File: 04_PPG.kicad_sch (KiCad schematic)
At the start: 0 parts

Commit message: updated schematics
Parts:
- added C4101, C4201: 22uF, Capacitor_SMD:C_0402_1005Metric, symbol Device:C
- added C4102, C4202: 100nF, Capacitor_SMD:C_0402_1005Metric, symbol Device:C
- added C4103, C4203: 1.0uF, Capacitor_SMD:C_0402_1005Metric, symbol Device:C
- added C4104, C4204: 10uF, Capacitor_SMD:C_0402_1005Metric, symbol Device:C
- added D401, D402: SFH7018A Q65113A6157, symbol sportwatch_custom:SFH7018A
- added D413, D414, D423, D424: SFH2703H Q65115A2199, symbol sportwatch_custom:SFH2703H
- added NT401: PPG1_PD_GND_TIE, symbol sportwatch_custom:NetTie_2
- added NT402: PPG2_PD_GND_TIE, symbol sportwatch_custom:NetTie_2
- added R401, R402, R405: 100k, Resistor_SMD:R_0402_1005Metric, symbol Device:R
- added R403, R404: 47k, Resistor_SMD:R_0402_1005Metric, symbol Device:R
- added U12, U13: MAX86141ENP+T, 21-100134_N201A2-1_MXM, symbol 2026-09-16_07-42-39:MAX86141ENP+T
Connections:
- new net GND: C4101.2, C4102.2, C4103.2, C4104.2, C4201.2, C4202.2, C4203.2, C4204.2, NT401.2 (B), NT402.2 (B), U12.C3 (GND_DIG), U12.C4 (GND_ANA), U12.D3 (PGND), U13.C3 (GND_DIG), U13.C4 (GND_ANA), U13.D3 (PGND)
- new net PPG1_CS_N: R401.2, U12.A5 (CSB)
- new net PPG1_INT_N: R403.2, U12.B2 (*INT)
- new net PPG1_LED_GREEN_DRV: D401.1 (K_GREEN_1), D401.8 (K_GREEN_3), U12.D1 (LED1_DRV)
- new net PPG1_LED_IR_DRV: D401.3 (K_IR), U12.B1 (LED3_DRV)
- new net PPG1_LED_RED_DRV: D401.5 (K_RED), U12.C1 (LED2_DRV)
- new net PPG1_PD1_IN: D413.1 (CATHODE), U12.D5 (PD1_IN)
- new net PPG1_PD2_IN: D414.1 (CATHODE), U12.D4 (PD2_IN)
- new net PPG1_PD_GND: D413.2 (ANODE), D414.2 (ANODE), NT401.1 (A), U12.C5 (PD_GND)
- new net PPG1_VREF: C4103.1, U12.B5 (VREF)
- new net PPG2_CS_N: R402.2, U13.A5 (CSB)
- new net PPG2_INT_N: R404.2, U13.B2 (*INT)
- new net PPG2_LED_GREEN_DRV: D402.1 (K_GREEN_1), D402.8 (K_GREEN_3), U13.D1 (LED1_DRV)
- new net PPG2_LED_IR_DRV: D402.3 (K_IR), U13.B1 (LED3_DRV)
- new net PPG2_LED_RED_DRV: D402.5 (K_RED), U13.C1 (LED2_DRV)
- new net PPG2_PD1_IN: D423.1 (CATHODE), U13.D5 (PD1_IN)
- new net PPG2_PD2_IN: D424.1 (CATHODE), U13.D4 (PD2_IN)
- new net PPG2_PD_GND: D423.2 (ANODE), D424.2 (ANODE), NT402.1 (A), U13.C5 (PD_GND)
- new net PPG2_VREF: C4203.1, U13.B5 (VREF)
- new net PPG_SAMPLE_SYNC: R405.2, U12.B3 (GPIO1), U13.B3 (GPIO1)
- new net PPG_SPI_MISO: U12.A3 (SDO), U13.A3 (SDO)
- new net PPG_SPI_MOSI: U12.A4 (SDI), U13.A4 (SDI)
- new net PPG_SPI_SCLK: U12.A2 (SCLK), U13.A2 (SCLK)
- new net PPG_VLED: C4104.1, C4204.1, D401.2 (A_RED_IR_1), D401.4 (A_RED_IR_2), D401.6 (A_GREEN), D402.2 (A_RED_IR_1), D402.4 (A_RED_IR_2), D402.6 (A_GREEN), U12.A1 (VLED), U13.A1 (VLED)
- new net VOUT1_1V8: C4101.1, C4102.1, C4201.1, C4202.1, R401.1, R402.1, R403.1, R404.1, R405.1, U12.C2 (VDD_DIG), U12.D2 (VDD_ANA), U13.C2 (VDD_DIG), U13.D2 (VDD_ANA)
- no-connect marks 0 -> 2
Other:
- note added: "04_PPG — DUAL MAX86141 OPTICAL HR / SpO2 FRONT END — REV A"
- note added: "AFE architecture: both MAX86141 devices share SPI SCLK/MOSI/MISO; each has its own CS and active-low open-drain INT."
- note added: "CRITICAL PCB: fully shield each PD_IN with its corresponding PD_GND; no unrelated traces/vias through or over the PD_GND shield. Keep PD paths extremely short."
- note added: "Custom SFH7018A and SFH2703H symbols are embedded in this schematic; exact optical footprints are intentionally left for the footprint audit."
- note added: "GPIO1 of both AFEs is tied to PPG_SAMPLE_SYNC. Firmware can use GPIO_CTRL=1010; one falling edge starts one programmed sample on both AFEs. GPIO2 is NC because no external LED mux is used."
- note added: "Keep the complete PPG analog/optical region away from Wi-Fi/GNSS RF, display/high-speed buses, switchers, inductors and the haptic actuator. Optical barriers and source-detector spacing are mechanical-design items."
- note added: "LED mapping per AFE: LED1_DRV=GREEN, LED2_DRV=RED, LED3_DRV=IR. Each AFE drives one SFH7018A package and receives two SFH2703H photodiodes."
- note added: "MAX86141 imported WLP footprint is retained for now. ALL three custom optical footprints plus WLP ball orientation are verified during the dedicated pre-PCB footprint audit."
- note added: "PD_GND1/2 are separate shield/reference nets and join PCB GND only through NT401/NT402. Use real net-tie copper/footprints, not resistors, during PCB footprint/layout audit."
- note added: "PPG_VLED is intentionally an external 3.1-5.5 V rail. Exact low-noise boost/regulator is not frozen yet; do not connect this net directly to an unsuitable system rail."
- note added: "SFH7018A exact pad map embedded from OSRAM: 1/7/8 green cathode, 2/4 red+IR anode, 3 IR cathode, 5 red cathode, 6 green anode. SFH2703H symbol uses pin1 cathode, pin2 anode."
- note added: "VDD_ANA and VDD_DIG use the same VOUT1_1V8 rail and must be shorted locally at each WLP. ADI layout guidance calls for 22uF + 0.1uF combined decoupling and 1uF on VREF."
- title: (none) -> Rev-A — Optical PPG / HR / SpO2

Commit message: refactor(kicad): integrate Rev-A hierarchy and libraries
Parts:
- U12, U13: footprint 21-100134_N201A2-1_MXM -> sportwatch_custom:21-100134_N201A2-1_MXM
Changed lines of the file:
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@@
 		)
 	)
-	(label "PPG1_INT_N"
+	(hierarchical_label "PPG1_INT_N"
+		(shape output)
 		(at 59 40 0)
 		(effects
@@
 		)
 	)
-	(label "VOUT1_1V8"
+	(hierarchical_label "VOUT1_1V8"
+		(shape passive)
 		(at 125.04 72.39 0)
 		(effects
@@
 		)
 	)
-	(label "PPG_SAMPLE_SYNC"
+	(hierarchical_label "PPG_SAMPLE_SYNC"
+		(shape bidirectional)
 		(at 93 40 0)
 		(effects
@@
 		)
 	)
-	(label "PPG2_CS_N"
+	(hierarchical_label "PPG2_CS_N"
+		(shape input)
 		(at 42 40 0)
 		(effects
@@
 		)
 	)
-	(label "PPG1_CS_N"
+	(hierarchical_label "PPG1_CS_N"
+		(shape input)
 		(at 25 40 0)
 		(effects
@@
 		)
 	)
-	(label "PPG_SPI_MOSI"
+	(hierarchical_label "PPG_SPI_MOSI"
+		(shape input)
 		(at 30.23 128.27 180)
 		(effects
@@
 		)
 	)
-	(label "PPG_SPI_MISO"
+	(hierarchical_label "PPG_SPI_MISO"
+		(shape output)
 		(at 34.04 69.85 180)
 		(effects
@@
 		)
 	)
-	(label "PPG_SPI_SCLK"
+	(hierarchical_label "PPG_SPI_SCLK"
+		(shape input)
 		(at 30.23 123.19 180)
 		(effects
@@
 		)
 	)
-	(label "PPG2_INT_N"
+	(hierarchical_label "PPG2_INT_N"
+		(shape output)
 		(at 30.23 135.89 180)
 		(effects
@@
 			)
 		)
-		(property "Footprint" "21-100134_N201A2-1_MXM"
+		(property "Footprint" "sportwatch_custom:21-100134_N201A2-1_MXM"
 			(at 50.8 120.65 0)
 			(hide yes)
@@
 			)
 		)
-		(property "Footprint" "21-100134_N201A2-1_MXM"
+		(property "Footprint" "sportwatch_custom:21-100134_N201A2-1_MXM"
 			(at 54.61 64.77 0)
 			(hide yes)

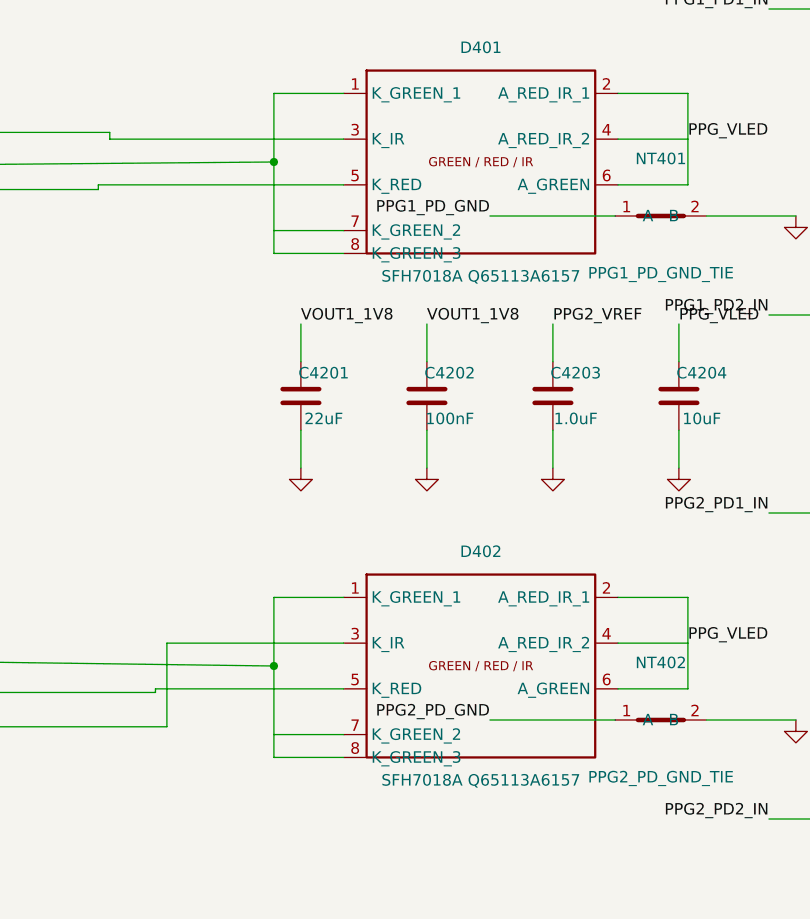
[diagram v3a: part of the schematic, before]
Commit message: fix(kicad): adjudicate and resolve native ERC errors
- Connect SFH7018A D401.7 and D402.7 green cathode pins to green LED drive
  nets per OSRAM pinout (Class A circuit fix)
- Add deliberate no_connect markers to unused pins U11.5 (QOD) and PMIC U201.15
  (SHPHLD), U201.28 (LSIN1), U201.30 (LSIN2) per datasheets (Class B)
- Place PWR_FLAG markers at external power sources: VBUSIN at J202, VBAT and
  GND at J201 (Class C)
- Place PWR_FLAG markers for net ties and post-inductor domains: PVSS1/PVSS2
  at NT201/NT202, PD_GND at NT401/NT402, and WIFI_VDD_BUCK at L601 (Class D)
- Correct symbol pin electrical types: nRF7002 PAVDD<0>/<1> to passive, PCA9306
  VREF2 to passive, and TC2030-CTX-NL nRESET to passive (Class E)
- Retain U12.A1/U13.A1 PPG_VLED undriven error as intentional TBD (Class G)
- Verification: 83/83 hierarchy interfaces match; ERC errors reduced from 18 to 1
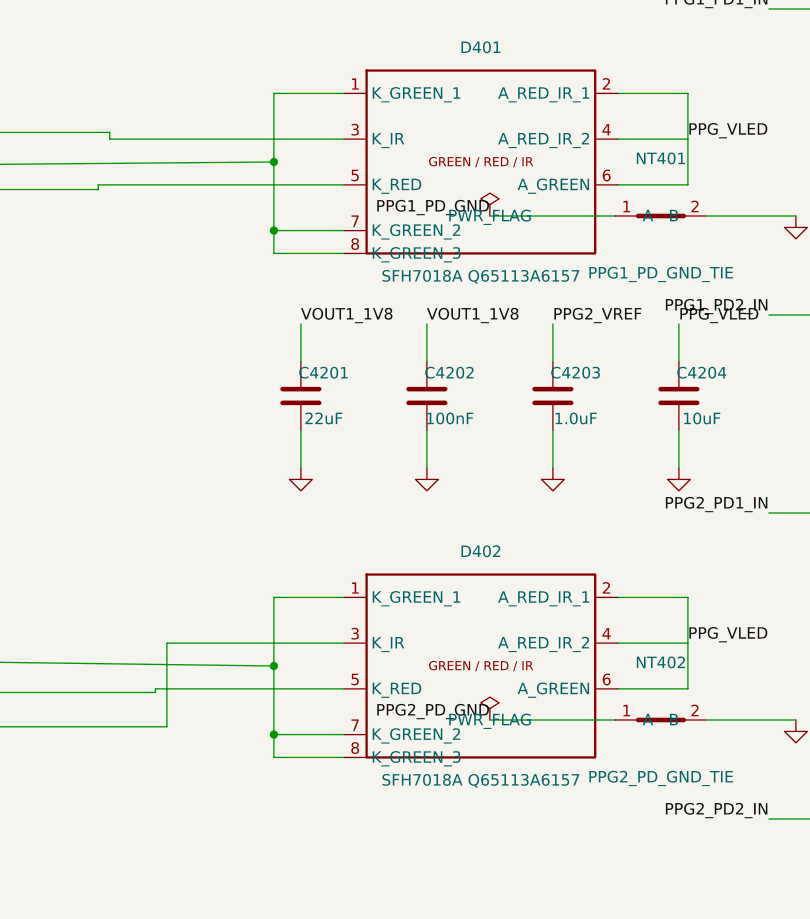
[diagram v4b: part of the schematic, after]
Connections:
- net PPG1_LED_GREEN_DRV: now also D401.7 (K_GREEN_2)
- net PPG2_LED_GREEN_DRV: now also D402.7 (K_GREEN_2)
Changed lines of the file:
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@@
 		)
 	)
+	(junction
+		(at 202 159.62)
+		(diameter 0)
+		(color 0 0 0 0)
+	)
+	(wire
+		(pts
+			(xy 202 152) (xy 202 159.62)
+		)
+		(stroke
+			(width 0)
+			(type default)
+		)
+	)
 	(wire
 		(pts
-			(xy 202 152) (xy 202 162.16)
+			(xy 202 159.62) (xy 202 162.16)
 		)
 		(stroke
@@
 		)
 	)
+	(junction
+		(at 202 103.62)
+		(diameter 0)
+		(color 0 0 0 0)
+	)
 	(wire
 		(pts
-			(xy 202 96) (xy 202 106.16)
+			(xy 202 96) (xy 202 103.62)
+		)
+		(stroke
+			(width 0)
+			(type default)
+		)
+	)
+	(wire
+		(pts
+			(xy 202 103.62) (xy 202 106.16)
 		)
 		(stroke
@@
 					(unit 1)
 				)
+			)
+		)
+	)
+	(symbol
+		(lib_id "power:PWR_FLAG")
+		(at 226 102 0)
+		(unit 1)
+		(body_style 1)
+		(exclude_from_sim no)
+		(in_bom yes)
+		(on_board yes)
+		(in_pos_files yes)
+		(dnp no)
+		(fields_autoplaced yes)
+		(property "Reference" "#FLG0401"
+			(at 226 102 0)
+			(hide yes)
+			(show_name no)
+			(do_not_autoplace no)
+			(effects
+				(font
+					(size 1.27 1.27)
+				)
+			)
+		)
+		(property "Value" "PWR_FLAG"
+			(at 226 102 0)
+			(show_name no)
+			(do_not_autoplace no)
+			(effects
+				(font
+					(size 1.27 1.27)
+				)
+			)
+		)
+		(property "Footprint" ""
+			(at 226 102 0)
+			(hide yes)
+			(show_name no)
+			(do_not_autoplace no)
+			(effects
+				(font
+					(size 1.27 1.27)
+				)
+			)
+		)
+		(property "Datasheet" ""
+			(at 226 102 0)
+			(hide yes)
+			(show_name no)
+			(do_not_autoplace no)
+			(effects
+				(font
+					(size 1.27 1.27)
+				)
+			)
+		)
+		(property "Description" ""
+			(at 226 102 0)
+			(hide yes)
+			(show_name no)
+			(do_not_autoplace no)
+			(effects
+				(font
+					(size 1.27 1.27)
+				)
+			)
+		)
+		(pin "1"
+		)
+		(instances
+			(project "sportwatch_revA"
+				(path "/063f9d99-6c07-44cf-ba32-e33897e06972/24ba7fae-0267-4a43-a776-43c6f8c3d7fc"
+					(reference "#FLG0401")
+					(unit 1)
+				)
+			)
+		)
+	)
+	(symbol
+		(lib_id "power:PWR_FLAG")
+		(at 226 158 0)
+		(unit 1)
+		(body_style 1)
+		(exclude_from_sim no)
+		(in_bom yes)
+		(on_board yes)
+		(in_pos_files yes)
+		(dnp no)
+		(fields_autoplaced yes)
+		(property "Reference" "#FLG0402"
+			(at 226 158 0)
+			(hide yes)
+			(show_name no)
+			(do_not_autoplace no)
+			(effects
+				(font
+					(size 1.27 1.27)
+				)
+			)
+		)
+		(property "Value" "PWR_FLAG"
+			(at 226 158 0)
+			(show_name no)
+			(do_not_autoplace no)
+			(effects
+				(font
+					(size 1.27 1.27)
+				)
+			)
+		)
+		(property "Footprint" ""
+			(at 226 158 0)
+			(hide yes)
+			(show_name no)
+			(do_not_autoplace no)
+			(effects
+				(font
+					(size 1.27 1.27)
+				)
+			)
+		)
+		(property "Datasheet" ""
+			(at 226 158 0)
+			(hide yes)
+			(show_name no)
+			(do_not_autoplace no)
+			(effects
+				(font
+					(size 1.27 1.27)
+				)
+			)
+		)
+		(property "Description" ""
+			(at 226 158 0)
+			(hide yes)
+			(show_name no)
+			(do_not_autoplace no)
+			(effects
+				(font
+					(size 1.27 1.27)
+				)
+			)
+		)
+		(pin "1"
+		)
+		(instances
+			(project "sportwatch_revA"
+				(path "/063f9d99-6c07-44cf-ba32-e33897e06972/24ba7fae-0267-4a43-a776-43c6f8c3d7fc"
+					(reference "#FLG0402")
+					(unit 1)
+				)

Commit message: froze schematics
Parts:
- added C401: 22uF, Capacitor_SMD:C_0603_1608Metric, symbol Device:C
- added C402: 47uF, Capacitor_SMD:C_0805_2012Metric, symbol Device:C
- added C403, C404, C405, C406, C407, C408: 100nF, symbol Device:C
- added D403, D404: SFH7018A Q65113A6157, symbol sportwatch_custom:SFH7018A
- added D405, D406, D407: SFH4053B Q65115A1586, symbol sportwatch_custom:SFH4053B
- added L401: 1uH, symbol Device:L
- added R406: 604k 1%, Resistor_SMD:R_0402_1005Metric, symbol Device:R
- added R407: 91k 1%, Resistor_SMD:R_0402_1005Metric, symbol Device:R
- added R408, R409: 10k, Resistor_SMD:R_0402_1005Metric, symbol Device:R
- added U401: TPS631000DRLR, symbol sportwatch_custom:TPS631000DRLR
- added U402, U403, U404, U405, U406, U407: TS5A12301E, symbol sportwatch_custom:TS5A12301E
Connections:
- net GND: now also C401.2, C402.2, C403.2, C404.2, C405.2, C406.2, C407.2, C408.2, R407.2, U401.6 (MODE), U401.7 (GND), U402.B1 (GND), U403.B1 (GND), U404.B1 (GND), U405.B1 (GND), U406.B1 (GND), U407.B1 (GND)
- net PPG1_LED_GREEN_DRV: now also U402.B2 (COM); no longer D401.1 (K_GREEN_1), D401.7 (K_GREEN_2), D401.8 (K_GREEN_3)
- net PPG1_LED_IR_DRV: now also U404.B2 (COM); no longer D401.3 (K_IR)
- net PPG1_LED_RED_DRV: now also U403.B2 (COM); no longer D401.5 (K_RED)
- net PPG2_LED_GREEN_DRV: now also U405.B2 (COM); no longer D402.1 (K_GREEN_1), D402.7 (K_GREEN_2), D402.8 (K_GREEN_3)
- net PPG2_LED_IR_DRV: now also U407.B2 (COM); no longer D402.3 (K_IR)
- net PPG2_LED_RED_DRV: now also U406.B2 (COM); no longer D402.5 (K_RED)
- net PPG_VLED: now also C402.1, C403.1, C404.1, C405.1, C406.1, C407.1, C408.1, D403.2 (A_RED_IR_1), D403.4 (A_RED_IR_2), D403.6 (A_GREEN), D404.2 (A_RED_IR_1), D404.4 (A_RED_IR_2), D404.6 (A_GREEN), D405.1 (ANODE), D406.1 (ANODE), D407.1 (ANODE), R406.1, U401.1 (VOUT), U402.C2 (VCC), U403.C2 (VCC), U404.C2 (VCC), U405.C2 (VCC), U406.C2 (VCC), U407.C2 (VCC)
- net VOUT1_1V8: now also R408.1, R409.1, U401.5 (EN)
- net PPG2_LED_MUX_SEL: now reaches U13.B4 (GPIO2)
- net PPG2_LED_MUX_SEL: now also R409.2, U405.A2 (IN), U406.A2 (IN), U407.A2 (IN)
- net PPG1_LED_MUX_SEL: now reaches U12.B4 (GPIO2)
- net PPG1_LED_MUX_SEL: now also R408.2, U402.A2 (IN), U403.A2 (IN), U404.A2 (IN)
- new net: L401.2, U401.2 (LX2)
- new net: L401.1, U401.3 (LX1)
- new net PPG1_LED1_GREEN_K: D401.1 (K_GREEN_1), D401.7 (K_GREEN_2), D401.8 (K_GREEN_3), U402.A1 (NO)
- new net PPG1_LED2_RED_K: D401.5 (K_RED), U403.A1 (NO)
- new net PPG1_LED3_IR850_K: D405.2 (CATHODE), U404.A1 (NO)
- new net PPG1_LED4_GREEN_K: D403.1 (K_GREEN_1), D403.7 (K_GREEN_2), D403.8 (K_GREEN_3), U402.C1 (NC)
- new net PPG1_LED5_RED_K: D403.5 (K_RED), U403.C1 (NC)
- new net PPG1_LED6_IR850_K: D406.2 (CATHODE), U404.C1 (NC)
- new net PPG2_LED1_GREEN_K: D402.1 (K_GREEN_1), D402.7 (K_GREEN_2), D402.8 (K_GREEN_3), U405.A1 (NO)
- new net PPG2_LED2_RED_K: D402.5 (K_RED), U406.A1 (NO)
- new net PPG2_LED3_IR850_K: D407.2 (CATHODE), U407.A1 (NO)
- new net PPG2_LED4_GREEN_K: D404.1 (K_GREEN_1), D404.7 (K_GREEN_2), D404.8 (K_GREEN_3), U405.C1 (NC)
- new net PPG2_LED5_RED_K: D404.5 (K_RED), U406.C1 (NC)
- new net PPG2_LED6_IR940_K: D402.3 (K_IR), U407.C1 (NC)
- new net PPG_FB: R406.2, R407.1, U401.8 (FB)
- new net VBAT: C401.1, U401.4 (VIN)
- no-connect marks 2 -> 3
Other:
- note added: "APPLE-INSPIRED 12-EMITTER PPG: 4x green, 4x red, 3x IR850, 1x IR940. Current Apple Ultra 4 exact emitter count is not publicly enumerated; this follows the documented Ultra/Ultra 2 wavelength mix within dual-MAX86141 12-LED capability."
- note added: "Apple-inspired optical architecture: 12 independently selected emitters total = 4 green + 4 red + 3 IR850 + 1 IR940, with the existing four SFH2703H photodiodes. Each MAX86141 uses a 3x2:1 LED mux bank."
- note added: "C401 22uF input, C402 47uF output + existing 10uF per AFE; R406 604k/R407 91k; L401 1uH DFE252012P-1R0M=P2 baseline."
- note added: "Custom SFH7018A, SFH4053B, SFH2703H and TS5A12301E symbols are embedded; exact new optical/mux footprints remain for the dedicated footprint audit."
- note added: "Firmware starting current caps: SFH4053B IR850 <=62mA; SFH7018A red <=31mA baseline; green/IR940 <=62mA baseline until optical/thermal/eye-safety validation."
- note added: "GPIO1 of both AFEs remains PPG_SAMPLE_SYNC. Use GPIO_CTRL=1010: falling GPIO1 starts one sample; GPIO2 is automatic external-mux control (HIGH for LED1/2/3, LOW for LED4/5/6)."
- note added: "PPG VLED POWER — TPS631000 buck-boost from protected VBAT, nominal 3.82V; EN=VOUT1_1V8, MODE=GND (PFM)."
- note added: "PPG_VLED is generated locally by U401 TPS631000 from protected VBAT. Nominal rail ~3.82 V; EN follows VOUT1_1V8. Keep VLED switching/layout away from PD_IN/PD_GND and optical analog nodes."
- note added: "TS5A12301E mux logic: GPIO2 HIGH -> NO = LED1/2/3; GPIO2 LOW -> NC = LED4/5/6. Power muxes from PPG_VLED; 1.8V GPIO control is supported."
- note removed: "Custom SFH7018A and SFH2703H symbols are embedded in this schematic; exact optical footprints are intentionally left for the footprint audit."
- note removed: "GPIO1 of both AFEs is tied to PPG_SAMPLE_SYNC. Firmware can use GPIO_CTRL=1010; one falling edge starts one programmed sample on both AFEs. GPIO2 is NC because no external LED mux is used."
- note removed: "LED mapping per AFE: LED1_DRV=GREEN, LED2_DRV=RED, LED3_DRV=IR. Each AFE drives one SFH7018A package and receives two SFH2703H photodiodes."
- note removed: "PPG_VLED is intentionally an external 3.1-5.5 V rail. Exact low-noise boost/regulator is not frozen yet; do not connect this net directly to an unsuitable system rail."

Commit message: feat(kicad): assign and audit Rev-A footprints
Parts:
- C403, C404, C405, C406, C407, C408: footprint (none) -> Capacitor_SMD:C_0402_1005Metric
- D401, D402, D403, D404: footprint (none) -> sportwatch_custom:OSRAM_SFH7018A_2.4x2.4mm
- D405, D406, D407: footprint (none) -> sportwatch_custom:OSRAM_SFH4053B_1.0x0.5mm
- D413, D414, D423, D424: footprint (none) -> sportwatch_custom:OSRAM_SFH2703_3.2x2.0mm
- L401: footprint (none) -> sportwatch_custom:L_2016_2016Metric
- NT401, NT402: footprint (none) -> NetTie:NetTie-2_SMD_Pad0.5mm
- U401: footprint (none) -> Package_TO_SOT_SMD:SOT-583-8
- U402, U403, U404, U405, U406, U407: footprint (none) -> Package_BGA:Texas_DSBGA-6_0.76x1.16mm_Layout2x3_P0.4mm

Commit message: fix(pcb): Round 3 foundation correction — 0 DRC errors, stacked microvias, PPG ECO & guards
- Eliminate 24 committed DRC errors by refilling all zones and committing refilled state
- Rebuild 12 L1->L3 skip microvias as 24 stackup-compliant stacked L1->L2 + L2->L3 microvias (VIPPO IPC-4761 Type VII)
- Harmonize HighSpeed_50R track width to 0.100 mm across .kicad_pro, .kicad_dru, and live copper
- Execute controlled schematic ECO swapping D413 and D424 detector channels, eliminating Jordan curve crossing
- Route all 4 PPG detector channels pad-to-pad on B.Cu with continuous dedicated PD_GND ground guards
- Close schematic residuals: Y101 MPN ABS07-32.768KHZ-6-T and 8.2pF load caps, cite primary sources for Y102 and Y1 on-chip trim, cite u-blox manual for U8 VCC_RF NC
- Formally defer staged passives (eMMC interface, PPG VLED, C206) with documented reserved placement corridors
- Document comprehensive Round 3 report and update Apollo/eMMC escape matrices and AGENT_HANDOFF.md
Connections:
- net PPG1_PD1_IN: now also D424.1 (CATHODE); no longer D413.1 (CATHODE)
- net PPG1_PD_GND: now also D424.2 (ANODE); no longer D413.2 (ANODE)
- net PPG2_PD2_IN: now also D413.1 (CATHODE); no longer D424.1 (CATHODE)
- net PPG2_PD_GND: now also D413.2 (ANODE); no longer D424.2 (ANODE)
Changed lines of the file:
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@@
+		)
+	)
+	(label "PPG2_PD_GND"
+		(at 290 79 0)
+		(effects
+			(font
+				(size 1.27 1.27)
+			)
+			(justify left bottom)
 		)
 	)
 	(label "PPG1_PD_GND"
-		(at 290 79 0)
-		(effects
-			(font
-				(size 1.27 1.27)
-			)
-			(justify left bottom)
-		)
-	)
-	(label "PPG2_PD_GND"
 		(at 290 169 0)
 		(effects
@@
 		)
 	)
-	(label "PPG2_PD2_IN"
+	(label "PPG1_PD1_IN"
 		(at 257 169 180)
 		(effects
@@
 		)
 	)
-	(label "PPG1_PD1_IN"
+	(label "PPG2_PD2_IN"
 		(at 257 79 180)
 		(effects
